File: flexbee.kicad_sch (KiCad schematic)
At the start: 68 parts, among them J1 Conn_01x12_Male, J2 Conn_01x12_Male, U1 SSD210, U2 ea3056, U3 spinor, Y1 Crystal_GND24

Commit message: schematic check
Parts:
- added R? (x2): R, Resistor_SMD:R_0402_1005Metric, symbol Device:R
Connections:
- net +3V3: now also R?.1, R?.1
- net ttl18: no longer J2.9 (Pin_9), U1.47 (ttl18)
- net ttl19: no longer J2.10 (Pin_10), U1.48 (ttl19)
- net i2c0_sda: now reaches U2.15 (SDA)
- net i2c0_sda: now also U1.48 (ttl19), R?.2
- net i2c0_scl: now reaches U2.16 (SCL)
- net i2c0_scl: now also U1.47 (ttl18), R?.2
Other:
- note added: "No decoupling caps?"
- note added: "Voltage level. Must be checked!"
- note added: "ttl18 and ttl19 used for i2c"
- moved on the sheet: C18, C20, C21, C5, C6, C7, C8, C9, L2, L3, R14, R15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

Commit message: Add files via upload
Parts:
- gave numbers to parts that had none: 2
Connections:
- net i2c0_scl: now also TP5.1, U1.29 (ttl0); no longer U1.47 (ttl18)
- net i2c0_sda: now also TP1.1, U1.30 (ttl1); no longer U1.48 (ttl19)
- net ttl18: now also J2.9 (Pin_9), U1.47 (ttl18)
- net ttl19: now also J2.10 (Pin_10), U1.48 (ttl19)
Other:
- note removed: "Voltage level. Must be checked!"
- note removed: "ttl18 and ttl19 used for i2c"
- moved on the sheet: C11, C13, R11, R18, R19, R9

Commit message: Add files via upload
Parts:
- added C24, C25, C26, C27, C28, C29, C30: C, Capacitor_SMD:C_0402_1005Metric, symbol Device:C
- added C31, C32, C33: C, Capacitor_SMD:C_0603_1608Metric, symbol Device:C
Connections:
- net +1V0: now also C25.1, C27.1, C28.1, C31.1
- net +1V8: now also C24.1, C32.1
- net +3V3: now also J1.1 (Pin_1), C26.1, C29.1, C30.1, C33.1; no longer J1.11 (Pin_11)
- net GND: now also C24.2, C25.2, C26.2, C27.2, C28.2, C29.2, C30.2, C31.2, C32.2, C33.2
- net VCC: now also J1.11 (Pin_11); no longer J1.1 (Pin_1)
- net lineout: now also J1.3 (Pin_3); no longer J1.10 (Pin_10)
- net sar_gpio0: now also J1.4 (Pin_4); no longer J1.3 (Pin_3)
- net sar_gpio1: now also J1.5 (Pin_5); no longer J1.4 (Pin_4)
- net sar_gpio2: now also J1.6 (Pin_6); no longer J1.5 (Pin_5)
- net ttl11: now also J2.12 (Pin_12); no longer J2.2 (Pin_2)
- net ttl12: now also J2.9 (Pin_9); no longer J2.3 (Pin_3)
- net ttl13: now also J2.10 (Pin_10); no longer J2.4 (Pin_4)
- net ttl14: now also J2.8 (Pin_8); no longer J2.5 (Pin_5)
- net ttl15: now also J2.7 (Pin_7); no longer J2.6 (Pin_6)
- net ttl16: now also J2.6 (Pin_6); no longer J2.7 (Pin_7)
- net ttl17: now also J2.5 (Pin_5); no longer J2.8 (Pin_8)
- net ttl18: now also J2.4 (Pin_4); no longer J2.9 (Pin_9)
- net ttl19: now also J2.3 (Pin_3); no longer J2.10 (Pin_10)
- net ttl20: now also J2.2 (Pin_2); no longer J2.11 (Pin_11)
- net ttl21: now also J2.1 (Pin_1); no longer J2.12 (Pin_12)
- net ttl8: now also J2.11 (Pin_11); no longer J2.1 (Pin_1)
- net uart_rx: now also J1.7 (Pin_7); no longer J1.6 (Pin_6)
- net uart_tx: now also J1.8 (Pin_8); no longer J1.7 (Pin_7)
- net usb_dm: now also J1.9 (Pin_9); no longer J1.8 (Pin_8)
- net usb_dp: now also J1.10 (Pin_10); no longer J1.9 (Pin_9)
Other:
- moved on the sheet: C11, C12, C13, C14, C15, C16, C22, R10, R11, R16, R18, R19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

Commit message: Finished laying you the board
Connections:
- net usb_dm renamed usb-
- net usb_dp renamed usb+
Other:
- note removed: "No decoupling caps?"
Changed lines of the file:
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@@
     (stroke (width 0) (type default) (color 0 0 0 0))
   )
-  (text "No decoupling caps?" (at 140.335 48.26 0)
-    (effects (font (size 1.27 1.27) (thickness 0.254) bold) (justify left bottom))
-  )
-  (label "usb_dm" (at 40.64 143.51 180)
+  (label "usb-" (at 40.64 143.51 180)
     (effects (font (size 1.27 1.27)) (justify right bottom))
   )
-  (label "usb_dp" (at 218.44 199.39 0)
+  (label "usb+" (at 218.44 199.39 0)
     (effects (font (size 1.27 1.27)) (justify left bottom))
   )
@@
     (effects (font (size 1.27 1.27)) (justify right bottom))
   )
-  (label "usb_dm" (at 218.44 196.85 0)
+  (label "usb-" (at 218.44 196.85 0)
     (effects (font (size 1.27 1.27)) (justify left bottom))
   )
@@
     (effects (font (size 1.27 1.27)) (justify left bottom))
   )
-  (label "usb_dp" (at 40.64 140.97 180)
+  (label "usb+" (at 40.64 140.97 180)
     (effects (font (size 1.27 1.27)) (justify right bottom))
   )

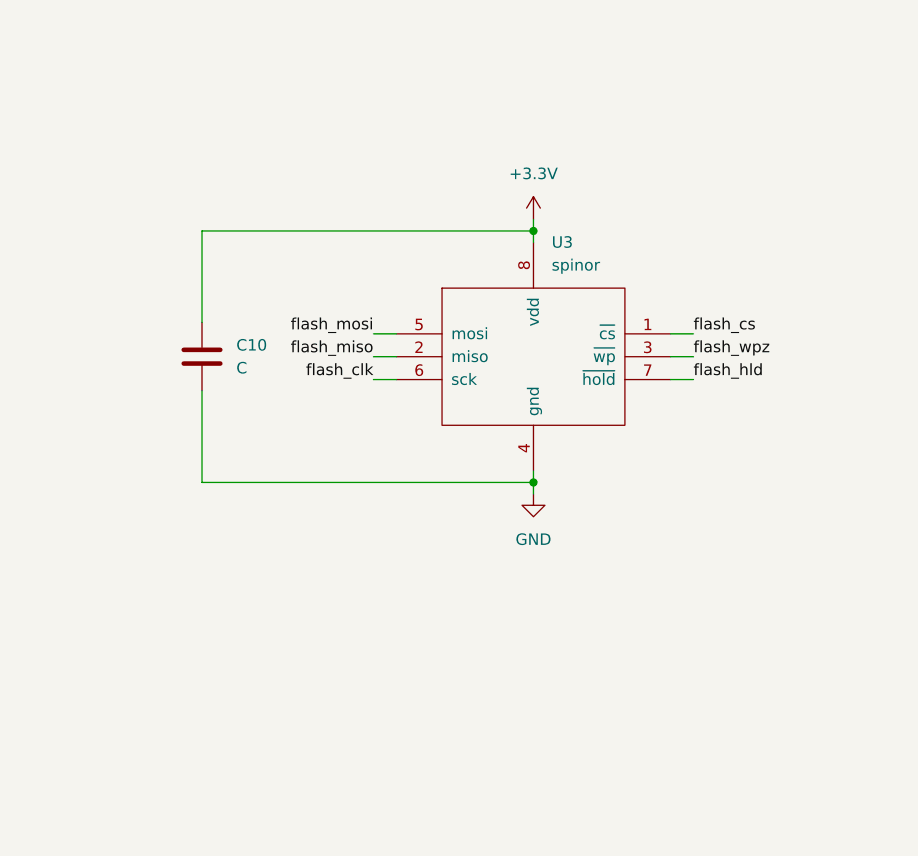
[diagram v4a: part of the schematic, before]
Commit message: Update flexbee.kicad_sch
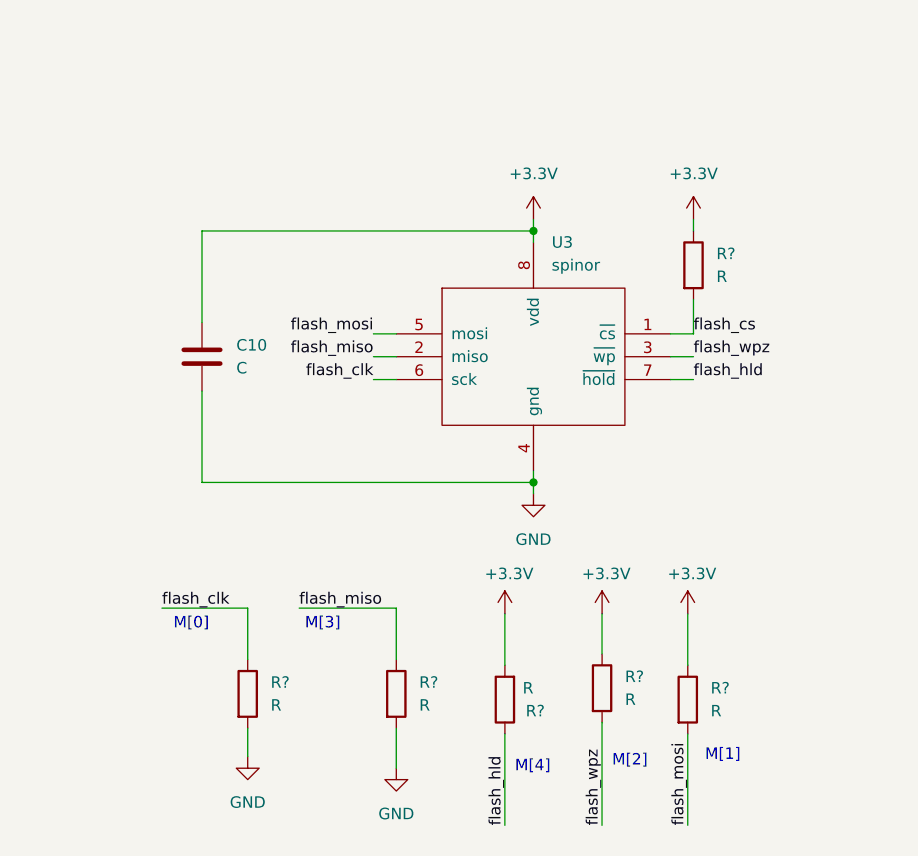
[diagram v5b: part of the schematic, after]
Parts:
- added R? (x6): R, Capacitor_SMD:C_0402_1005Metric, symbol Device:R
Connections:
- net +3V3: now also R?.1, R?.1, R?.1, R?.2
- net GND: now also R?.2, R?.2
- net flash_clk: now also R?.1
- net flash_cs: now also R?.2
- net flash_hld: now also R?.1
- net flash_miso: now also R?.1
- net flash_mosi: now also R?.2
- net flash_wpz: now also R?.2
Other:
- note added: "M[0]"
- note added: "M[1]"
- note added: "M[2]"
- note added: "M[3]"
- note added: "M[4]"

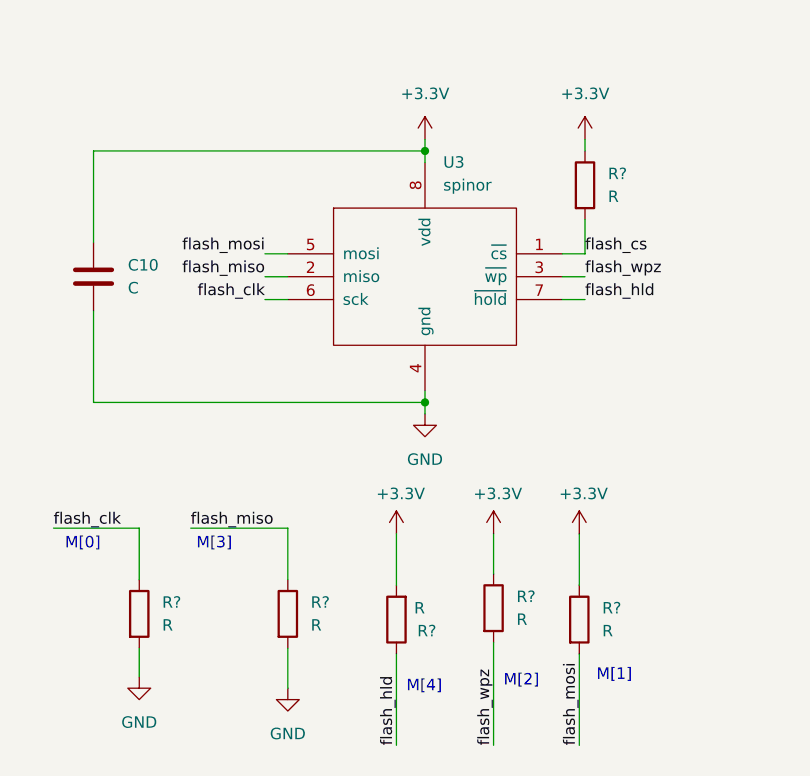
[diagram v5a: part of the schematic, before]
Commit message: Update boot resistors added
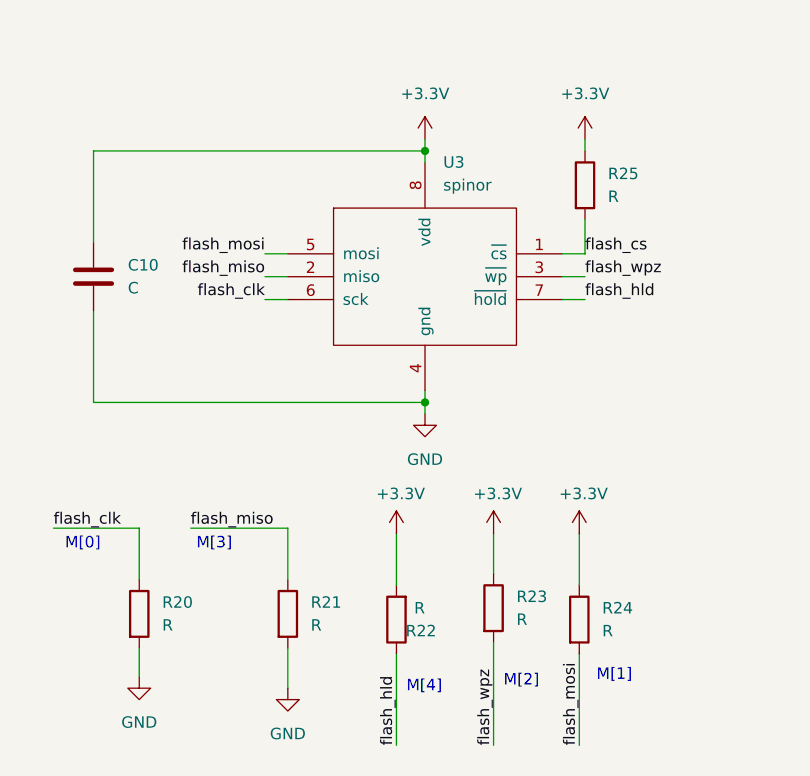
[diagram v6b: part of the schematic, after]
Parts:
- gave numbers to parts that had none: 6
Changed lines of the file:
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@@
   (symbol (lib_id "Device:R") (at 361.315 222.25 0) (unit 1)
     (in_bom yes) (on_board yes) (fields_autoplaced)
-    (property "Reference" "R?" (id 0) (at 363.855 220.9799 0)
+    (property "Reference" "R24" (id 0) (at 363.855 220.9799 0)
       (effects (font (size 1.27 1.27)) (justify left))
     )
@@
   (symbol (lib_id "power:+3.3V") (at 361.315 212.725 0) (unit 1)
     (in_bom yes) (on_board yes)
-    (property "Reference" "#PWR?" (id 0) (at 361.315 216.535 0)
+    (property "Reference" "#PWR014" (id 0) (at 361.315 216.535 0)
       (effects (font (size 1.27 1.27)) hide)
     )
@@
   (symbol (lib_id "power:+3.3V") (at 361.95 168.91 0) (unit 1)
     (in_bom yes) (on_board yes) (fields_autoplaced)
-    (property "Reference" "#PWR?" (id 0) (at 361.95 172.72 0)
+    (property "Reference" "#PWR015" (id 0) (at 361.95 172.72 0)
       (effects (font (size 1.27 1.27)) hide)
     )
@@
   (symbol (lib_id "Device:R") (at 340.995 222.25 180) (unit 1)
     (in_bom yes) (on_board yes)
-    (property "Reference" "R?" (id 0) (at 345.44 223.52 0)
+    (property "Reference" "R22" (id 0) (at 345.44 223.52 0)
       (effects (font (size 1.27 1.27)) (justify left))
     )
@@
   (symbol (lib_id "power:GND") (at 328.93 229.87 0) (unit 1)
     (in_bom yes) (on_board yes) (fields_autoplaced)
-    (property "Reference" "#PWR?" (id 0) (at 328.93 236.22 0)
+    (property "Reference" "#PWR011" (id 0) (at 328.93 236.22 0)
       (effects (font (size 1.27 1.27)) hide)
     )
@@
   (symbol (lib_id "power:GND") (at 312.42 228.6 0) (unit 1)
     (in_bom yes) (on_board yes) (fields_autoplaced)
-    (property "Reference" "#PWR?" (id 0) (at 312.42 234.95 0)
+    (property "Reference" "#PWR010" (id 0) (at 312.42 234.95 0)
       (effects (font (size 1.27 1.27)) hide)
     )
@@
   (symbol (lib_id "Device:R") (at 351.79 220.98 0) (unit 1)
     (in_bom yes) (on_board yes) (fields_autoplaced)
-    (property "Reference" "R?" (id 0) (at 354.33 219.7099 0)
+    (property "Reference" "R23" (id 0) (at 354.33 219.7099 0)
       (effects (font (size 1.27 1.27)) (justify left))
     )
@@
   (symbol (lib_id "Device:R") (at 361.95 173.99 0) (unit 1)
     (in_bom yes) (on_board yes) (fields_autoplaced)
-    (property "Reference" "R?" (id 0) (at 364.49 172.7199 0)
+    (property "Reference" "R25" (id 0) (at 364.49 172.7199 0)
       (effects (font (size 1.27 1.27)) (justify left))
     )
@@
   (symbol (lib_id "Device:R") (at 312.42 221.615 0) (unit 1)
     (in_bom yes) (on_board yes) (fields_autoplaced)
-    (property "Reference" "R?" (id 0) (at 314.96 220.3449 0)
+    (property "Reference" "R20" (id 0) (at 314.96 220.3449 0)
       (effects (font (size 1.27 1.27)) (justify left))
     )
@@
   (symbol (lib_id "Device:R") (at 328.93 221.615 0) (unit 1)
     (in_bom yes) (on_board yes) (fields_autoplaced)
-    (property "Reference" "R?" (id 0) (at 331.47 220.3449 0)
+    (property "Reference" "R21" (id 0) (at 331.47 220.3449 0)
       (effects (font (size 1.27 1.27)) (justify left))
     )
@@
   (symbol (lib_id "power:+3.3V") (at 351.79 212.725 0) (unit 1)
     (in_bom yes) (on_board yes)
-    (property "Reference" "#PWR?" (id 0) (at 351.79 216.535 0)
+    (property "Reference" "#PWR013" (id 0) (at 351.79 216.535 0)
       (effects (font (size 1.27 1.27)) hide)
     )
@@
   (symbol (lib_id "power:+3.3V") (at 340.995 212.725 0) (unit 1)
     (in_bom yes) (on_board yes)
-    (property "Reference" "#PWR?" (id 0) (at 340.995 216.535 0)
+    (property "Reference" "#PWR012" (id 0) (at 340.995 216.535 0)
       (effects (font (size 1.27 1.27)) hide)
     )
@@
       (reference "#PWR09") (unit 1) (value "GND") (footprint "")
     )
+    (path "/4d67b37b-0afa-41ec-a729-55f53a8a19b2"
+      (reference "#PWR010") (unit 1) (value "GND") (footprint "")
+    )
+    (path "/3fe8fb23-de15-4bbf-977a-51555d1947fe"
+      (reference "#PWR011") (unit 1) (value "GND") (footprint "")
+    )
+    (path "/f994202c-05ff-47fc-b011-935abf07aa23"
+      (reference "#PWR012") (unit 1) (value "+3.3V") (footprint "")
+    )
+    (path "/c0436b4d-68ca-448d-9915-68c6171f56e4"
+      (reference "#PWR013") (unit 1) (value "+3.3V") (footprint "")
+    )
+    (path "/1f48933e-112a-4e8b-9540-672780ace741"
+      (reference "#PWR014") (unit 1) (value "+3.3V") (footprint "")
+    )
+    (path "/23816596-419f-4368-b2cd-464259dc5b86"
+      (reference "#PWR015") (unit 1) (value "+3.3V") (footprint "")
+    )
     (path "/76cc1b59-e67d-45ab-bf21-ce86b013da2e"
       (reference "#PWR0101") (unit 1) (value "GND") (footprint "")
@@
       (reference "#PWR0127") (unit 1) (value "+1V0") (footprint "")
     )
-    (path "/1f48933e-112a-4e8b-9540-672780ace741"
-      (reference "#PWR?") (unit 1) (value "+3.3V") (footprint "")
-    )
-    (path "/23816596-419f-4368-b2cd-464259dc5b86"
-      (reference "#PWR?") (unit 1) (value "+3.3V") (footprint "")
-    )
-    (path "/3fe8fb23-de15-4bbf-977a-51555d1947fe"
-      (reference "#PWR?") (unit 1) (value "GND") (footprint "")
-    )
-    (path "/4d67b37b-0afa-41ec-a729-55f53a8a19b2"
-      (reference "#PWR?") (unit 1) (value "GND") (footprint "")
-    )
-    (path "/c0436b4d-68ca-448d-9915-68c6171f56e4"
-      (reference "#PWR?") (unit 1) (value "+3.3V") (footprint "")
-    )
-    (path "/f994202c-05ff-47fc-b011-935abf07aa23"
-      (reference "#PWR?") (unit 1) (value "+3.3V") (footprint "")
-    )
     (path "/238e82ef-dd4f-4432-bfc0-7a9a17cde23c"
       (reference "C1") (unit 1) (value "C") (footprint "Capacitor_SMD:C_0402_1005Metric")
@@
       (reference "R19") (unit 1) (value "R") (footprint "Resistor_SMD:R_0402_1005Metric")
     )
+    (path "/a25af48e-dbeb-4028-9fa8-64d527309bba"
+      (reference "R20") (unit 1) (value "R") (footprint "Capacitor_SMD:C_0402_1005Metric")
+    )
+    (path "/b5219c58-7234-4c26-805d-2815118102c3"
+      (reference "R21") (unit 1) (value "R") (footprint "Capacitor_SMD:C_0402_1005Metric")
+    )
+    (path "/2bc53ec8-4ad0-44dc-a811-556dfa58e94f"
+      (reference "R22") (unit 1) (value "R") (footprint "Capacitor_SMD:C_0402_1005Metric")
+    )
+    (path "/67725315-f002-458f-9979-9509618bd274"
+      (reference "R23") (unit 1) (value "R") (footprint "Capacitor_SMD:C_0402_1005Metric")
+    )
     (path "/1c44698e-43b2-4c3e-af04-9f4c3a704687"
-      (reference "R?") (unit 1) (value "R") (footprint "Capacitor_SMD:C_0402_1005Metric")
-    )
-    (path "/2bc53ec8-4ad0-44dc-a811-556dfa58e94f"
-      (reference "R?") (unit 1) (value "R") (footprint "Capacitor_SMD:C_0402_1005Metric")
-    )
-    (path "/67725315-f002-458f-9979-9509618bd274"
-      (reference "R?") (unit 1) (value "R") (footprint "Capacitor_SMD:C_0402_1005Metric")
+      (reference "R24") (unit 1) (value "R") (footprint "Capacitor_SMD:C_0402_1005Metric")
     )
     (path "/85322899-72eb-4118-9f75-1f66b01e7b34"
-      (reference "R?") (unit 1) (value "R") (footprint "Capacitor_SMD:C_0402_1005Metric")
-    )
-    (path "/a25af48e-dbeb-4028-9fa8-64d527309bba"
-      (reference "R?") (unit 1) (value "R") (footprint "Capacitor_SMD:C_0402_1005Metric")
-    )
-    (path "/b5219c58-7234-4c26-805d-2815118102c3"
-      (reference "R?") (unit 1) (value "R") (footprint "Capacitor_SMD:C_0402_1005Metric")
+      (reference "R25") (unit 1) (value "R") (footprint "Capacitor_SMD:C_0402_1005Metric")
     )
     (path "/7d243791-ebeb-481f-962f-83aec7081e2d"

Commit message: Sync with my local machine
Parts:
- C10, C12, C14, C15, C16, C22, C24, C25, C26, C27, C28, C29, C3, C30, C4, C6, C7: value C -> 1uF
- C17, C18: value C -> 18pF
- C31, C32, C33: value C -> 1uf
- R1, R8: value R -> 100k
- R10: value R -> 1.2M; footprint Capacitor_SMD:C_0402_1005Metric -> Resistor_SMD:R_0402_1005Metric
- R11, R25, R9: footprint Capacitor_SMD:C_0402_1005Metric -> Resistor_SMD:R_0402_1005Metric
- R12: value R -> 1m; footprint Capacitor_SMD:C_0402_1005Metric -> Resistor_SMD:R_0402_1005Metric
- R13: value R -> 1.1m
- R14, R15: value R -> 1m
- R18, R19: value R -> 4.7K
- R2: value R -> 150k
- R20, R21, R22, R23, R24: value R -> 4.7K; footprint Capacitor_SMD:C_0402_1005Metric -> Resistor_SMD:R_0402_1005Metric
- R5: value R -> 510k
- R6: value R -> 110k
- R7: value R -> 200k

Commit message: Sync
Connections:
- net VCC: now also C3.1, U2.23 (LDO_I)
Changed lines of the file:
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@@
   (junction (at 181.61 72.39) (diameter 0) (color 0 0 0 0)
   )
+  (junction (at 255.27 46.99) (diameter 0) (color 0 0 0 0)
+  )
   (junction (at 205.74 60.96) (diameter 0) (color 0 0 0 0)
   )
@@
   (junction (at 255.27 39.37) (diameter 0) (color 0 0 0 0)
   )
+  (junction (at 246.38 57.15) (diameter 0) (color 0 0 0 0)
+  )
   (junction (at 63.5 229.87) (diameter 0) (color 0 0 0 0)
   )
@@
     (stroke (width 0) (type default) (color 0 0 0 0))
   )
+  (wire (pts (xy 246.38 46.99) (xy 255.27 46.99))
+    (stroke (width 0) (type default) (color 0 0 0 0))
+  )
   (wire (pts (xy 222.25 41.91) (xy 222.25 44.45))
     (stroke (width 0) (type default) (color 0 0 0 0))
@@
     (stroke (width 0) (type default) (color 0 0 0 0))
   )
+  (wire (pts (xy 246.38 57.15) (xy 246.38 46.99))
+    (stroke (width 0) (type default) (color 0 0 0 0))
+  )
   (wire (pts (xy 168.275 81.28) (xy 168.275 94.615))
     (stroke (width 0) (type default) (color 0 0 0 0))
@@
     (stroke (width 0) (type default) (color 0 0 0 0))
   )
+  (wire (pts (xy 255.27 46.99) (xy 255.27 76.2))
+    (stroke (width 0) (type default) (color 0 0 0 0))
+  )
   (wire (pts (xy 390.525 68.58) (xy 400.685 68.58))
     (stroke (width 0) (type default) (color 0 0 0 0))
@@
     (stroke (width 0) (type default) (color 0 0 0 0))
   )
-  (wire (pts (xy 255.27 39.37) (xy 255.27 76.2))
-    (stroke (width 0) (type default) (color 0 0 0 0))
-  )
+  (wire (pts (xy 255.27 39.37) (xy 255.27 46.99))
+    (stroke (width 0) (type default) (color 0 0 0 0))
+  )
